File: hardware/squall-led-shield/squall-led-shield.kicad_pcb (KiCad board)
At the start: 2 copper layers, 9 parts, among them J1 SQUALL_HEADER, Q1 Q_2NMOS

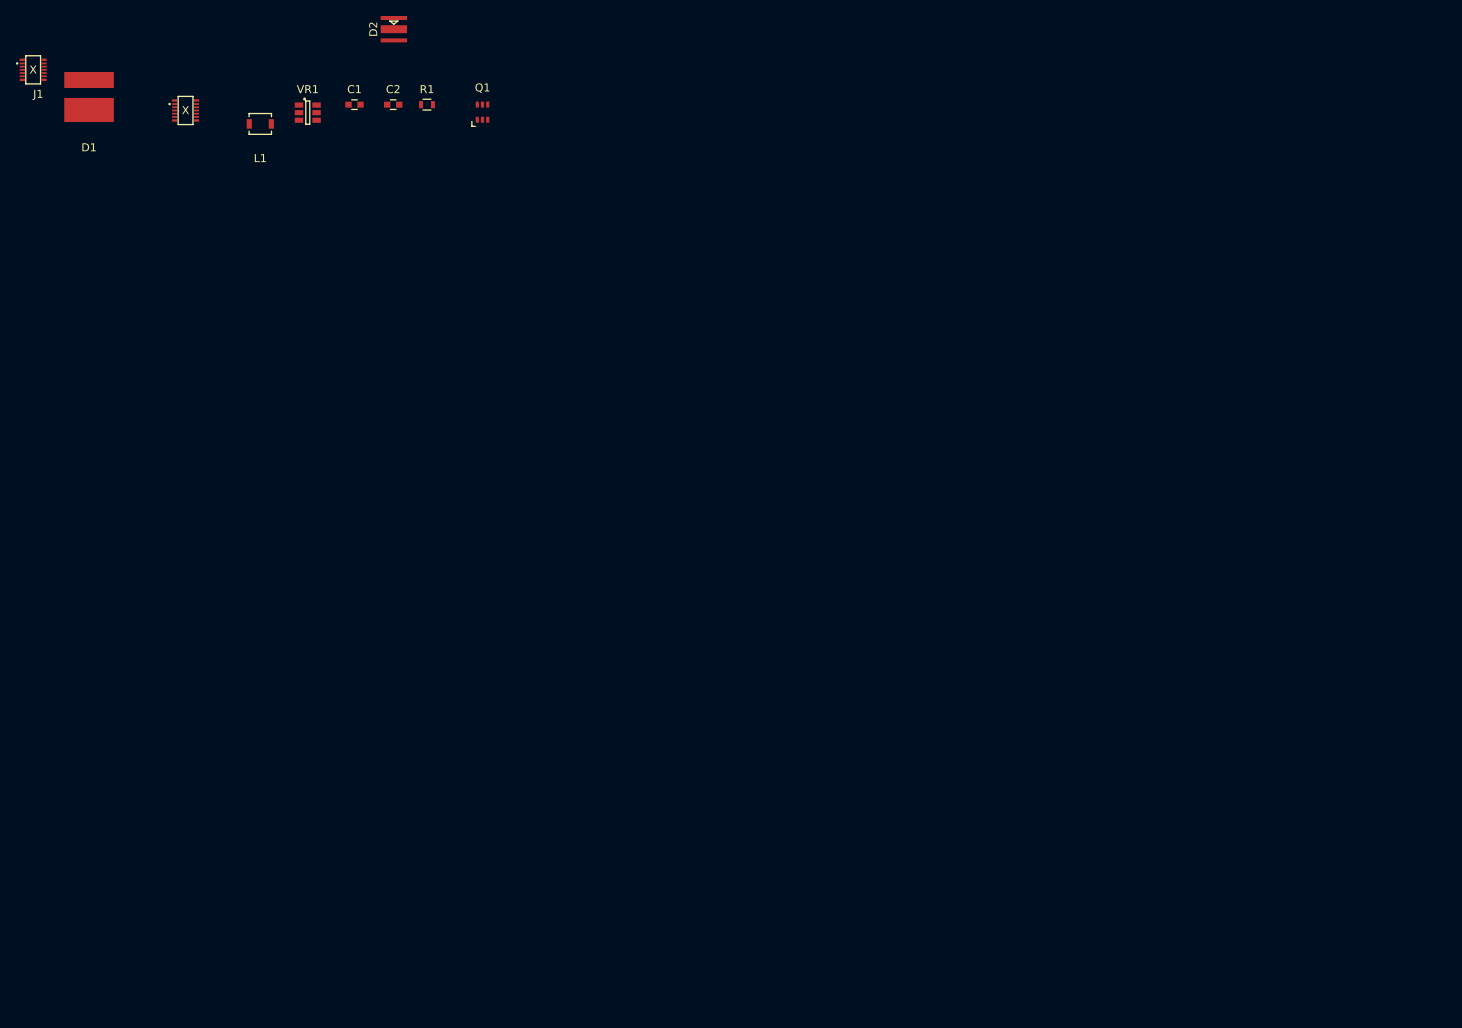
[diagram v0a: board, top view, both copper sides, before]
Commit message: Put Squall headers on both sides of the board
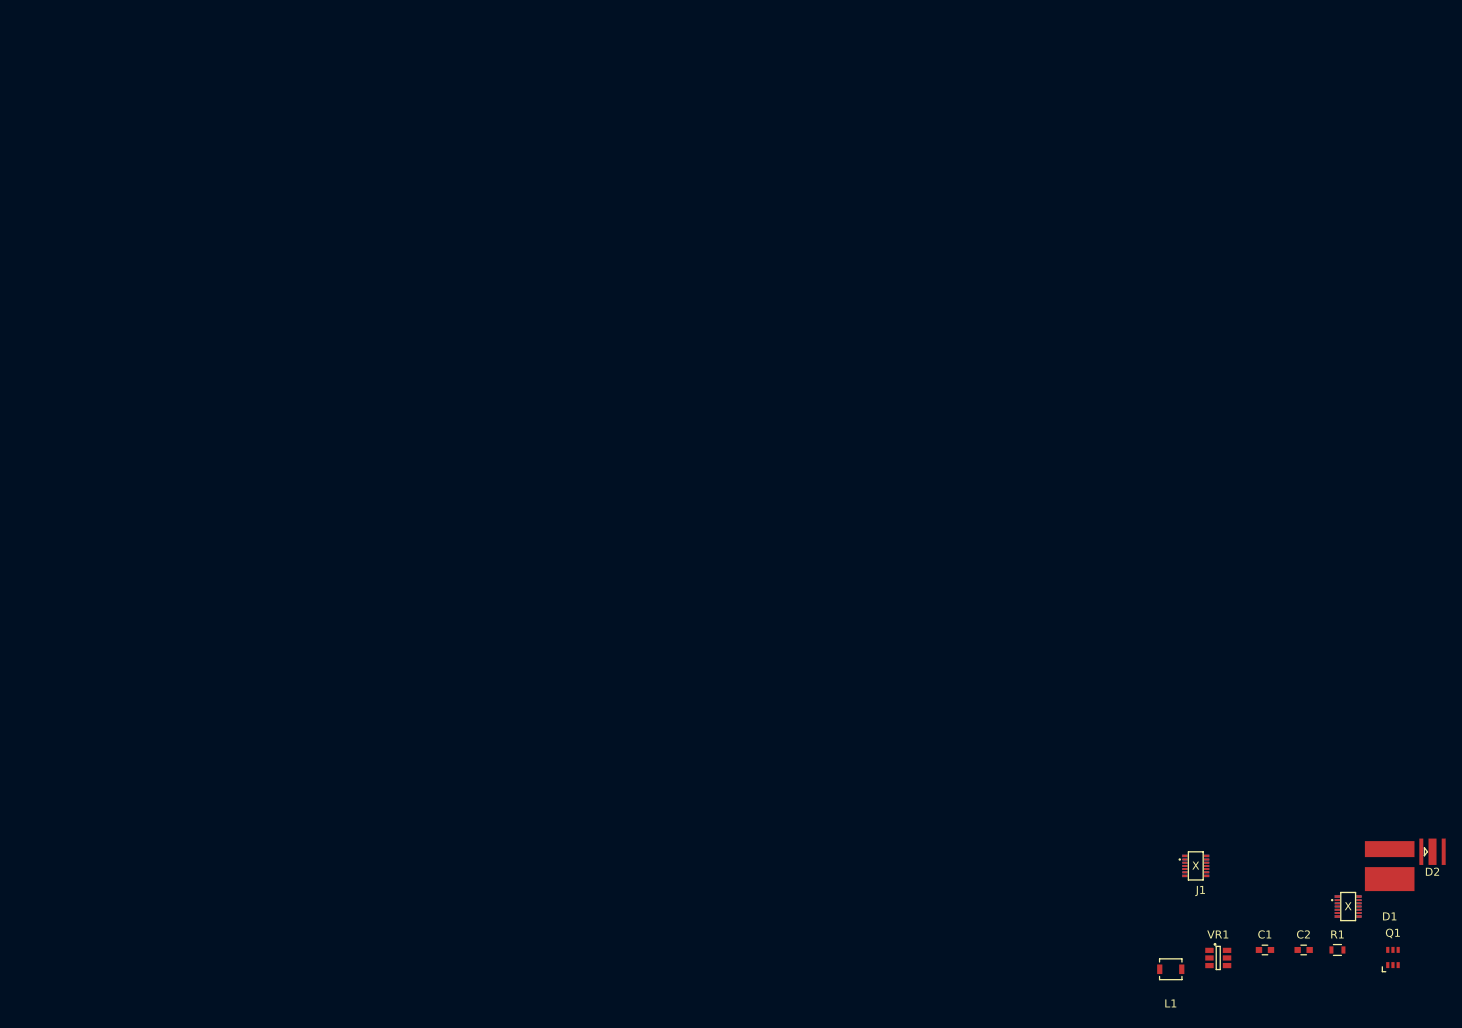
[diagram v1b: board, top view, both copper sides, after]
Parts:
- moved D1 188.9 mm to (160.0, 97.0)
- moved J1 176.1 mm to (145.3, 99.5)
- moved D2 165.6 mm to (165.4, 95.2), turned to 0 degrees
- moved C1 155.3 mm to (144.4, 107.5)
- moved C2 155.3 mm to (149.3, 107.5)
- moved L1 155.3 mm to (132.7, 109.9)
- moved Q1 155.3 mm to (160.5, 108.4)
- moved R1 155.3 mm to (153.5, 107.5)
- moved VR1 155.3 mm to (138.6, 108.5)
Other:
- net class Default: via_dia 0.762 -> 0.8128; via_drill 0.381 -> 0.4064
- rule pad_to_mask_clearance: 0.2 -> 0
- rule via_min_drill: 0.3302 -> 0.1524
- rule via_min_size: 0.6858 -> 0.1524

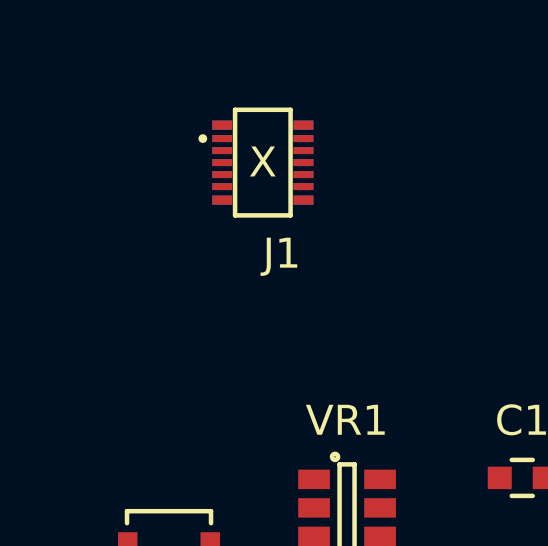
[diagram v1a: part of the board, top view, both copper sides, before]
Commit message: Add missing footprint for R2
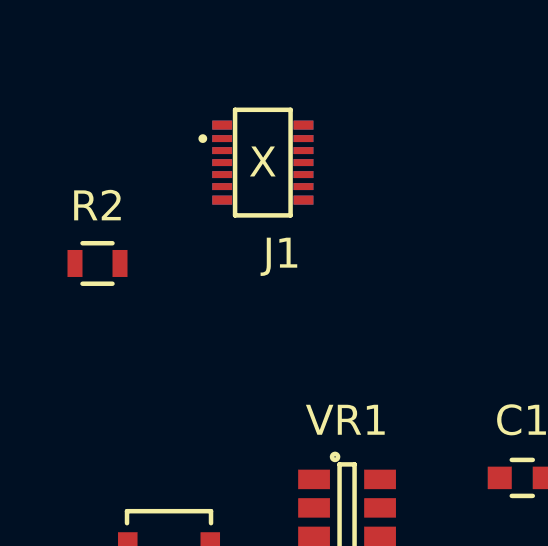
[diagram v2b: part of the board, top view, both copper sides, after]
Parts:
- added R2: 18Ω, Resistors_SMD:R_0603, F.Cu at (130.3, 100.3)
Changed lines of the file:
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@@
 (kicad_pcb (version 4) (host pcbnew "(2016-07-14 BZR 6979)-product")
   (general
-    (links 36)
-    (no_connects 36)
+    (links 37)
+    (no_connects 37)
     (area 0 0 0 0)
     (thickness 1.6)
-    (drawings 0)
+    (drawings 3)
     (tracks 0)
     (zones 0)
-    (modules 9)
-    (nets 26)
+    (modules 10)
+    (nets 27)
   )
   (page A4)
@@
   (net 24 "Net-(D2-Pad1)")
   (net 25 "Net-(VR1-Pad3)")
+  (net 26 "Net-(D2-Pad2)")
   (net_class Default "This is the default net class."
     (clearance 0.2032)
@@
     (add_net "Net-(D1-Pad2)")
     (add_net "Net-(D2-Pad1)")
+    (add_net "Net-(D2-Pad2)")
     (add_net "Net-(J1-Pad11)")
     (add_net "Net-(J1-Pad12)")
@@
       (at (xyz 0 0 0))
       (scale (xyz 1 1 1))
+      (rotate (xyz 0 0 0))
+    )
+  )
+  (module Resistors_SMD:R_0603 (layer F.Cu)
+    (at 130.29 100.33)
+    (descr "Resistor SMD 0603, reflow soldering, Vishay (see dcrcw.pdf)")
+    (tags "resistor 0603")
+    (attr smd)
+    (fp_text reference R2 (at 0 -1.9) (layer F.SilkS)
+      (effects (font (size 1 1) (thickness 0.15)))
+    )
+    (fp_text value 18Ω (at 0 1.9) (layer F.Fab)
+      (effects (font (size 1 1) (thickness 0.15)))
+    )
+    (fp_line (start -1.3 -0.8) (end 1.3 -0.8) (layer F.CrtYd) (width 0.05))
+    (fp_line (start -1.3 0.8) (end 1.3 0.8) (layer F.CrtYd) (width 0.05))
+    (fp_line (start -1.3 -0.8) (end -1.3 0.8) (layer F.CrtYd) (width 0.05))
+    (fp_line (start 1.3 -0.8) (end 1.3 0.8) (layer F.CrtYd) (width 0.05))
+    (fp_line (start 0.5 0.675) (end -0.5 0.675) (layer F.SilkS) (width 0.15))
+    (fp_line (start -0.5 -0.675) (end 0.5 -0.675) (layer F.SilkS) (width 0.15))
+    (pad 1 smd rect (at -0.75 0) (size 0.5 0.9) (layers F.Cu F.Paste F.Mask)
+      (net 3 /V3P6))
+    (pad 2 smd rect (at 0.75 0) (size 0.5 0.9) (layers F.Cu F.Paste F.Mask)
+      (net 26 "Net-(D2-Pad2)"))
+    (model Resistors_SMD.3dshapes/R_0603.wrl
+      (at (xyz 0 0 0))
+      (scale (xyz 1 1 1))

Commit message: WIP: Place parts
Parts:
- J1: value SQUALL_HEADER -> (none)
- moved L1 26.2 mm to (154.9, 96.0), turned to 90 degrees
- moved D2 21.3 mm to (148.1, 107.6), turned to 270 degrees
- moved R2 21.2 mm to (151.4, 102.6), turned to 270 degrees
- moved VR1 16.6 mm to (149.6, 96.0), turned to 270 degrees
- moved Q1 13.5 mm to (148.1, 103.1), turned to 180 degrees
- moved D1 11.4 mm to (156.0, 107.6), turned to 180 degrees
- moved C1 11.1 mm to (151.4, 98.8)
- moved C2 8.72 mm to (148.3, 98.8), turned to 180 degrees
- moved J1 7.38 mm to (152.4, 101.6)
- moved R1 5.50 mm to (154.7, 102.1), turned to 180 degrees
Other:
- board outline added: 25.4 x 21 mm

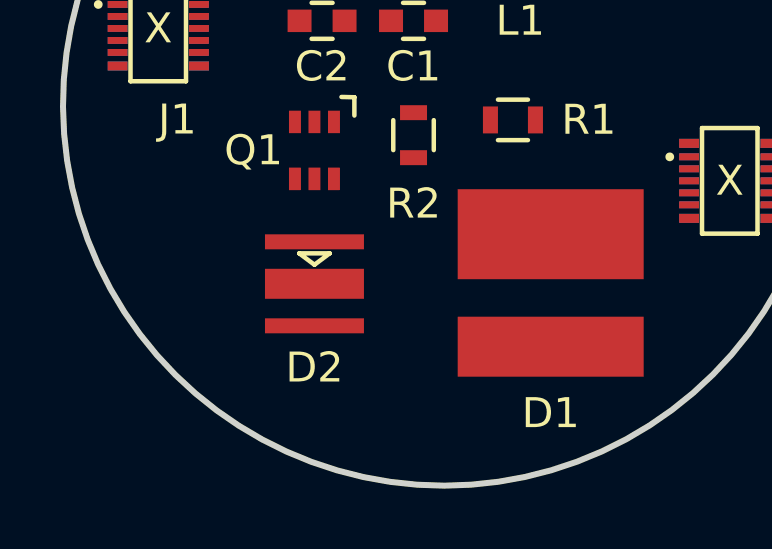
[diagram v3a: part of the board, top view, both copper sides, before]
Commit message: Fix pad names for CREE LED
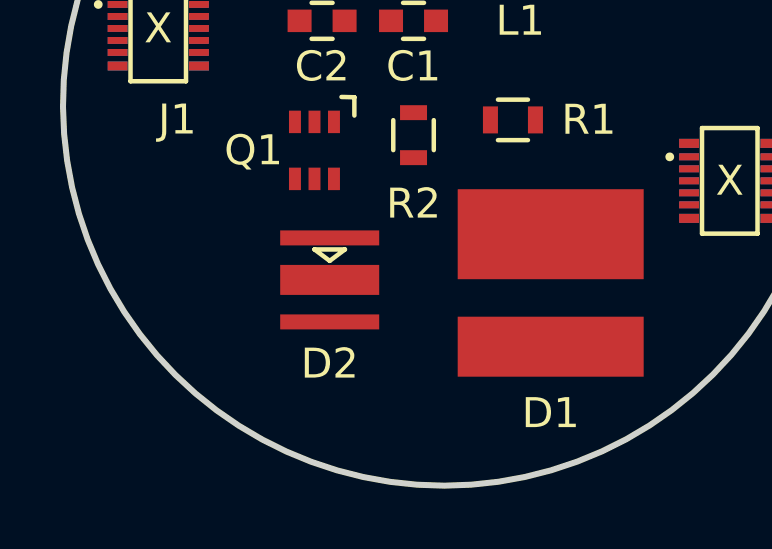
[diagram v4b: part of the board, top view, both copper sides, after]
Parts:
- J1: value (none) -> SQUALL_HEADER
- moved D2 0.52 mm to (148.6, 107.4)
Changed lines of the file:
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@@
 (kicad_pcb (version 4) (host pcbnew "(2016-07-14 BZR 6979)-product")
   (general
-    (links 37)
-    (no_connects 37)
-    (area 0 0 0 0)
+    (links 39)
+    (no_connects 39)
+    (area 139.599364 93.244999 165.200636 114.400636)
     (thickness 1.6)
     (drawings 3)
@@
       (net 5 "Net-(D1-Pad2)"))
   )
-  (module Squall:CREE_XT-E (layer F.Cu)
-    (at 148.082 107.572 270)
-    (fp_text reference D2 (at 2.794 0 360) (layer F.SilkS)
-      (effects (font (size 1 1) (thickness 0.15)))
-    )
-    (fp_text value LED (at 0 -2.54 270) (layer F.Fab) hide
-      (effects (font (size 1 1) (thickness 0.15)))
-    )
-    (fp_line (start -1.778 -1.778) (end 1.778 -1.778) (layer F.Fab) (width 0.15))
-    (fp_line (start 1.778 -1.778) (end 1.778 1.778) (layer F.Fab) (width 0.15))
-    (fp_line (start 1.778 1.778) (end -1.778 1.778) (layer F.Fab) (width 0.15))
-    (fp_line (start -1.778 1.778) (end -1.778 -1.778) (layer F.Fab) (width 0.15))
-    (fp_line (start -1.016 -0.508) (end -1.016 0.508) (layer F.SilkS) (width 0.15))
-    (fp_line (start -1.016 0.508) (end -0.635 0) (layer F.SilkS) (width 0.15))
-    (fp_line (start -0.635 0) (end -1.016 -0.508) (layer F.SilkS) (width 0.15))
-    (pad ANOD smd rect (at -1.4 0 270) (size 0.5 3.3) (layers F.Cu F.Paste F.Mask))
-    (pad CATH smd rect (at 1.4 0 270) (size 0.5 3.3) (layers F.Cu F.Paste F.Mask))
-    (pad THER smd rect (at 0 0 270) (size 1 3.3) (layers F.Cu F.Paste F.Mask))
-  )
   (module Squall:SQUALL_HEADER (layer F.Cu)
     (at 152.4 101.6)
@@
       (effects (font (size 1 1) (thickness 0.15)))
     )
-    (fp_text value "" (at -8.89 -6.85) (layer F.Fab)
+    (fp_text value SQUALL_HEADER (at -8.89 -6.85) (layer F.Fab)
       (effects (font (size 1 1) (thickness 0.15)))
     )
@@
     (tags SOT-23-6)
     (attr smd)
-    (fp_text reference VR1 (at 0 2.54 450) (layer F.SilkS)
+    (fp_text reference VR1 (at 0 2.54 90) (layer F.SilkS)
       (effects (font (size 1 1) (thickness 0.15)))
     )
@@
     (tags "resistor 0603")
     (attr smd)
-    (fp_text reference R2 (at 2.286 0 360) (layer F.SilkS)
+    (fp_text reference R2 (at 2.286 0) (layer F.SilkS)
       (effects (font (size 1 1) (thickness 0.15)))
     )
@@
     )
   )
+  (module Squall:CREE_XT-E (layer F.Cu)
+    (at 148.59 107.442 270)
+    (fp_text reference D2 (at 2.794 0 360) (layer F.SilkS)
+      (effects (font (size 1 1) (thickness 0.15)))
+    )
+    (fp_text value LED (at 0 -2.54 270) (layer F.Fab) hide
+      (effects (font (size 1 1) (thickness 0.15)))
+    )
+    (fp_line (start -1.778 -1.778) (end 1.778 -1.778) (layer F.Fab) (width 0.15))
+    (fp_line (start 1.778 -1.778) (end 1.778 1.778) (layer F.Fab) (width 0.15))
+    (fp_line (start 1.778 1.778) (end -1.778 1.778) (layer F.Fab) (width 0.15))
+    (fp_line (start -1.778 1.778) (end -1.778 -1.778) (layer F.Fab) (width 0.15))
+    (fp_line (start -1.016 -0.508) (end -1.016 0.508) (layer F.SilkS) (width 0.15))
+    (fp_line (start -1.016 0.508) (end -0.635 0) (layer F.SilkS) (width 0.15))
+    (fp_line (start -0.635 0) (end -1.016 -0.508) (layer F.SilkS) (width 0.15))
+    (pad 1 smd rect (at -1.4 0 270) (size 0.5 3.3) (layers F.Cu F.Paste F.Mask)
+      (net 24 "Net-(D2-Pad1)"))
+    (pad 2 smd rect (at 1.4 0 270) (size 0.5 3.3) (layers F.Cu F.Paste F.Mask)
+      (net 26 "Net-(D2-Pad2)"))
+    (pad THER smd rect (at 0 0 270) (size 1 3.3) (layers F.Cu F.Paste F.Mask))
+  )
   (gr_line (start 142.748 93.345) (end 162.052 93.345) (layer Edge.Cuts) (width 0.2))
